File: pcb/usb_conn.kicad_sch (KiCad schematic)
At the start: 5 parts

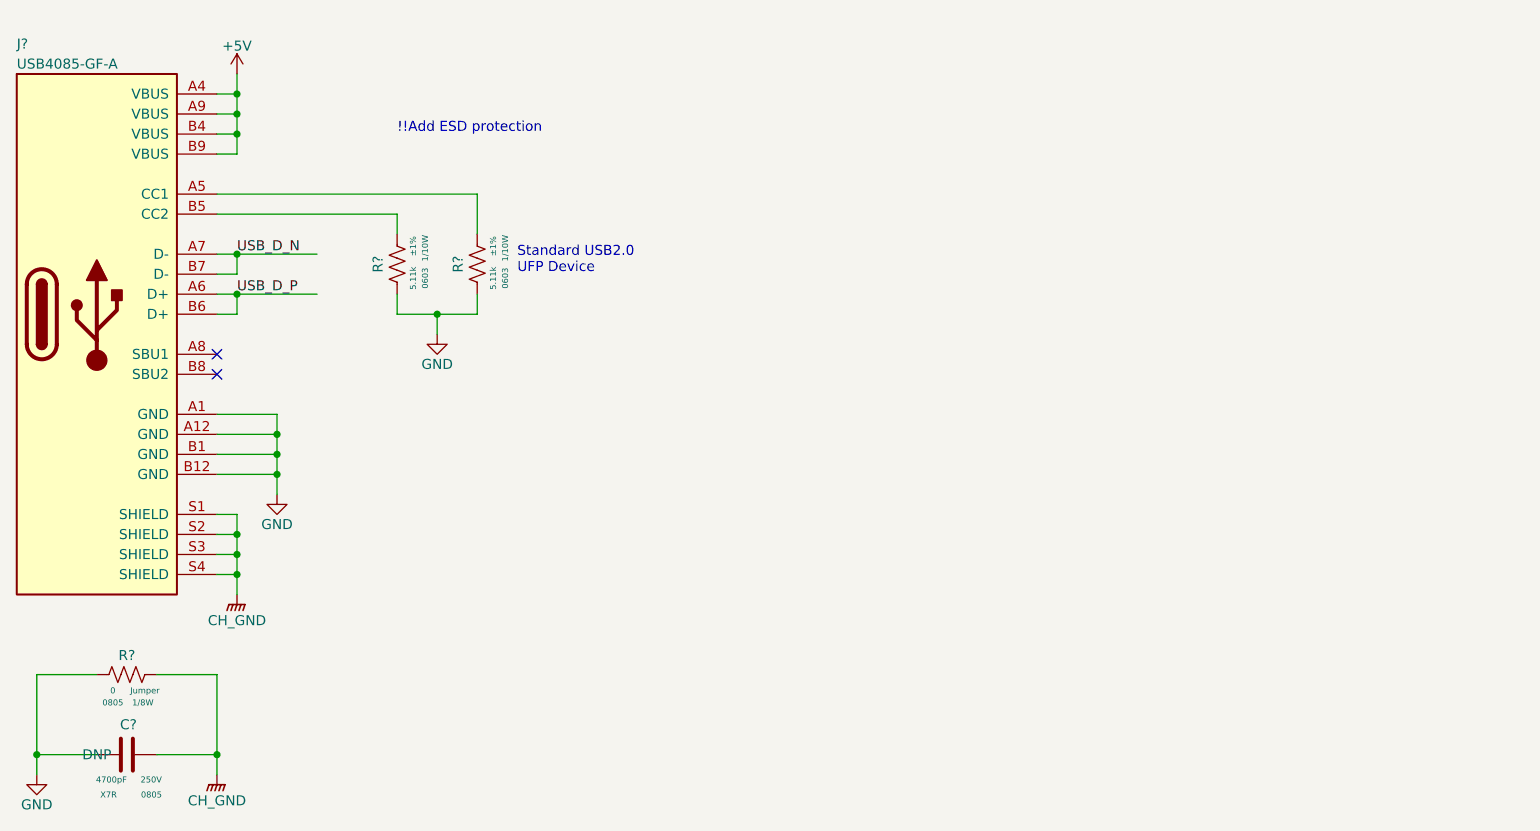
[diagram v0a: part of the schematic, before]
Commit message: Added IN-3 dots, picked FTDI chip and 3.3V LDO
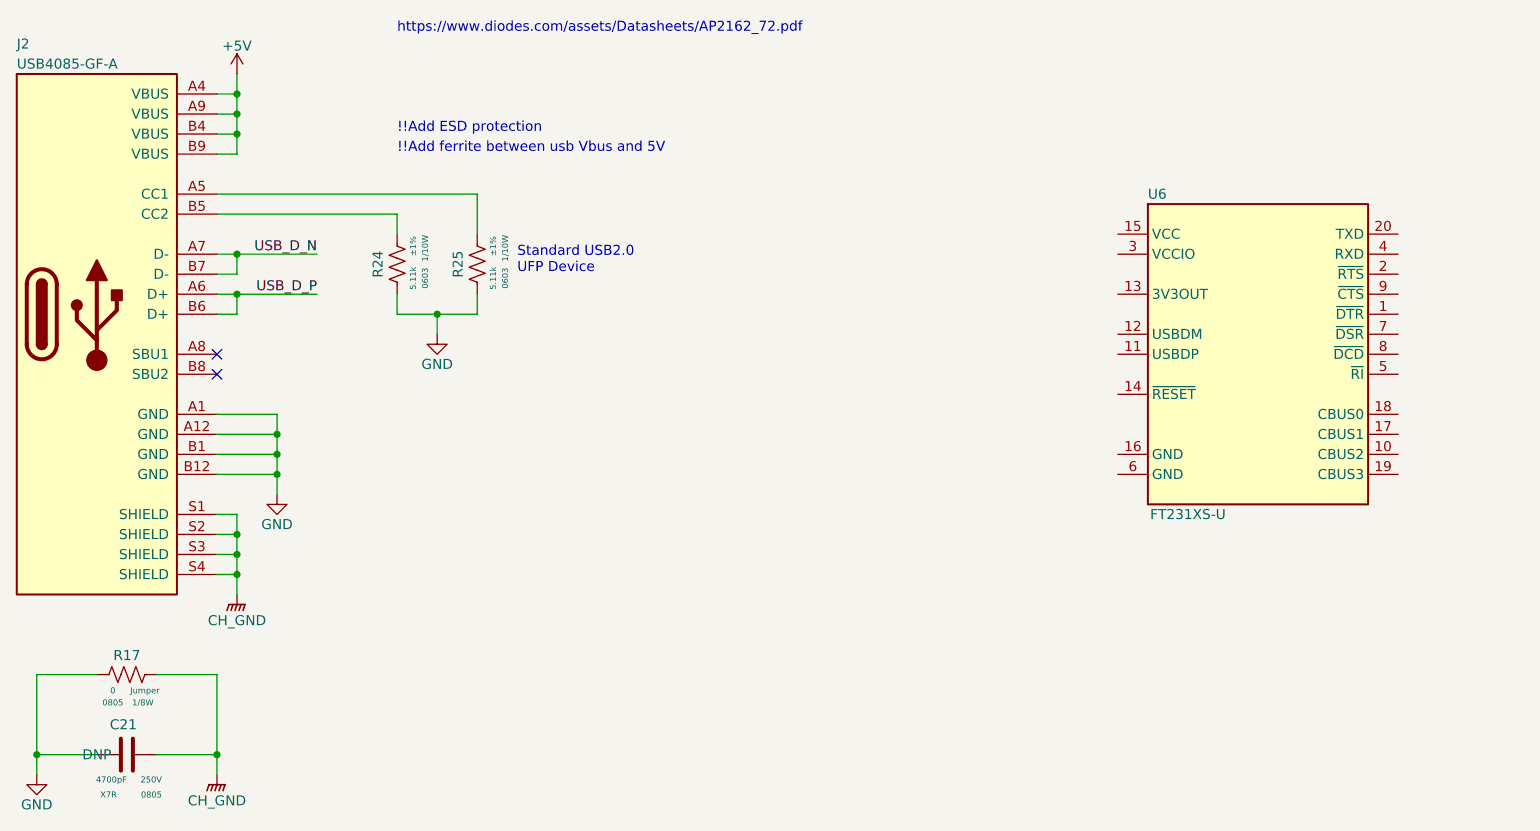
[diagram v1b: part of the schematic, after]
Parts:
- added U6: IC_FTDI_FT231XS, Package_SO:SSOP-20_3.9x8.7mm_P0.635mm, symbol arjun_symbols:IC_FTDI_FT231XS
- gave numbers to parts that had none: 5
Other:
- note added: "!!Add ferrite between usb Vbus and 5V"
- note added: "https://www.diodes.com/assets/Datasheets/AP2162_72.pdf"
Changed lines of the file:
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@@
+    (effects (font (size 1.27 1.27)) (justify left bottom))
+  )
+  (text "!!Add ferrite between usb Vbus and 5V" (at 78.74 71.12 0)
+    (effects (font (size 1.27 1.27)) (justify left bottom))
+  )
+  (text "https://www.diodes.com/assets/Datasheets/AP2162_72.pdf"
+    (at 78.74 55.88 0)
     (effects (font (size 1.27 1.27)) (justify left bottom))
   )
@@
     (effects (font (size 1.27 1.27)) (justify left bottom))
   )
-  (label "USB_D_P" (at 58.42 88.9 0)
-    (effects (font (size 1.27 1.27)) (justify left bottom))
-  )
-  (label "USB_D_N" (at 58.42 83.82 0)
-    (effects (font (size 1.27 1.27)) (justify left bottom))
+  (label "USB_D_P" (at 68.58 88.9 180)
+    (effects (font (size 1.27 1.27)) (justify right bottom))
+  )
+  (label "USB_D_N" (at 68.58 83.82 180)
+    (effects (font (size 1.27 1.27)) (justify right bottom))
   )
   (hierarchical_label "UART_BL_TX" (shape input) (at 251.46 93.98 0)
@@
   (symbol (lib_id "arjun_symbols:CH_GND") (at 58.42 127 0) (unit 1)
     (in_bom yes) (on_board yes)
-    (property "Reference" "#PWR?" (id 0) (at 58.42 132.08 0)
+    (property "Reference" "#PWR046" (id 0) (at 58.42 132.08 0)
       (effects (font (size 1.27 1.27)) hide)
     )
@@
   (symbol (lib_id "arjun_symbols:RES_5K11_1P_1{slash}10W_0603") (at 88.9 81.28 0) (unit 1)
     (in_bom yes) (on_board yes)
-    (property "Reference" "R?" (id 0) (at 85.725 85.09 90)
+    (property "Reference" "R25" (id 0) (at 85.725 85.09 90)
       (effects (font (size 1.27 1.27)) (justify top))
     )
@@
   (symbol (lib_id "power:+5V") (at 58.42 60.96 0) (unit 1)
     (in_bom yes) (on_board yes)
-    (property "Reference" "#PWR?" (id 0) (at 58.42 64.77 0)
+    (property "Reference" "#PWR045" (id 0) (at 58.42 64.77 0)
       (effects (font (size 1.27 1.27)) hide)
     )
@@
   (symbol (lib_id "arjun_symbols:RES_0R_1{slash}8W_0805") (at 48.26 137.16 270) (unit 1)
     (in_bom yes) (on_board yes)
-    (property "Reference" "R?" (id 0) (at 44.45 133.985 90)
+    (property "Reference" "R17" (id 0) (at 44.45 133.985 90)
       (effects (font (size 1.27 1.27)) (justify top))
     )
@@
   (symbol (lib_id "power:GND") (at 83.82 93.98 0) (unit 1)
     (in_bom yes) (on_board yes)
-    (property "Reference" "#PWR?" (id 0) (at 83.82 100.33 0)
+    (property "Reference" "#PWR055" (id 0) (at 83.82 100.33 0)
       (effects (font (size 1.27 1.27)) hide)
     )
@@
   (symbol (lib_id "arjun_symbols:CAP_CER_4700p_250V_X7R_0805") (at 40.64 147.32 90) (unit 1)
     (in_bom no) (on_board yes)
-    (property "Reference" "C?" (id 0) (at 45.72 143.51 90)
+    (property "Reference" "C21" (id 0) (at 45.72 143.51 90)
       (effects (font (size 1.27 1.27)) (justify left))
     )
@@
   (symbol (lib_id "arjun_symbols:CONN_USBC_RCPT_USB2.0_USB4085-GF-A") (at 55.88 63.5 0) (unit 1)
     (in_bom yes) (on_board yes)
-    (property "Reference" "J?" (id 0) (at 30.48 57.15 0)
+    (property "Reference" "J2" (id 0) (at 30.48 57.15 0)
       (effects (font (size 1.27 1.27)) (justify left))
     )
@@
   (symbol (lib_id "power:GND") (at 33.02 149.86 0) (unit 1)
     (in_bom yes) (on_board yes)
-    (property "Reference" "#PWR?" (id 0) (at 33.02 156.21 0)
+    (property "Reference" "#PWR043" (id 0) (at 33.02 156.21 0)
       (effects (font (size 1.27 1.27)) hide)
     )
@@
   (symbol (lib_id "arjun_symbols:RES_5K11_1P_1{slash}10W_0603") (at 78.74 81.28 0) (unit 1)
     (in_bom yes) (on_board yes)
-    (property "Reference" "R?" (id 0) (at 75.565 85.09 90)
+    (property "Reference" "R24" (id 0) (at 75.565 85.09 90)
       (effects (font (size 1.27 1.27)) (justify top))
     )
@@
   (symbol (lib_id "power:GND") (at 63.5 114.3 0) (unit 1)
     (in_bom yes) (on_board yes)
-    (property "Reference" "#PWR?" (id 0) (at 63.5 120.65 0)
+    (property "Reference" "#PWR047" (id 0) (at 63.5 120.65 0)
       (effects (font (size 1.27 1.27)) hide)
     )
@@
     (pin "1")
   )
+  (symbol (lib_id "arjun_symbols:IC_FTDI_FT231XS") (at 170.18 81.28 0) (unit 1)
+    (in_bom yes) (on_board yes)
+    (property "Reference" "U6" (id 0) (at 173.99 76.2 0)
+      (effects (font (size 1.27 1.27)) (justify left))
+    )
+    (property "Value" "IC_FTDI_FT231XS" (id 1) (at 231.14 63.5 0)
+      (effects (font (size 1.27 1.27)) (justify left) hide)
+    )
+    (property "Footprint" "Package_SO:SSOP-20_3.9x8.7mm_P0.635mm" (id 2) (at 254 66.04 0)
+      (effects (font (size 1.27 1.27)) hide)
+    )
+    (property "Datasheet" "https://www.ftdichip.com/Support/Documents/DataSheets/ICs/DS_FT231X.pdf" (id 3) (at 232.41 76.2 0)
+      (effects (font (size 1.27 1.27)) (justify left) hide)
+    )
+    (property "Manufacturer" "FTDI" (id 4) (at 232.41 78.74 0)
+      (effects (font (size 1.27 1.27)) (justify left) hide)
+    )
+    (property "ManufacturerPN" "FT231XS-U" (id 5) (at 179.07 116.84 0))
+    (property "Vendor" "Digi-Key" (id 6) (at 232.41 71.12 0)
+      (effects (font (size 1.27 1.27)) (justify left) hide)
+    )
+    (property "VendorPN" "768-1156-5-ND" (id 7) (at 232.41 73.66 0)
+      (effects (font (size 1.27 1.27)) (justify left) hide)
+    )
+    (pin "1")
+    (pin "10")
+    (pin "11")
+    (pin "12")
+    (pin "13")
+    (pin "14")
+    (pin "15")
+    (pin "16")
+    (pin "17")
+    (pin "18")
+    (pin "19")
+    (pin "2")
+    (pin "20")
+    (pin "3")
+    (pin "4")
+    (pin "5")
+    (pin "6")
+    (pin "7")
+    (pin "8")
+    (pin "9")
+  )
   (symbol (lib_id "arjun_symbols:CH_GND") (at 55.88 149.86 0) (unit 1)
     (in_bom yes) (on_board yes)
-    (property "Reference" "#PWR?" (id 0) (at 55.88 154.94 0)
-      (effects (font (size 1.27 1.27)) hide)
-    )
+    (property "Reference" "#PWR044" (id 0) (at 55.88 154.94 0)
+      (effects (font (size 1.27 1.27)) hide)
+    )

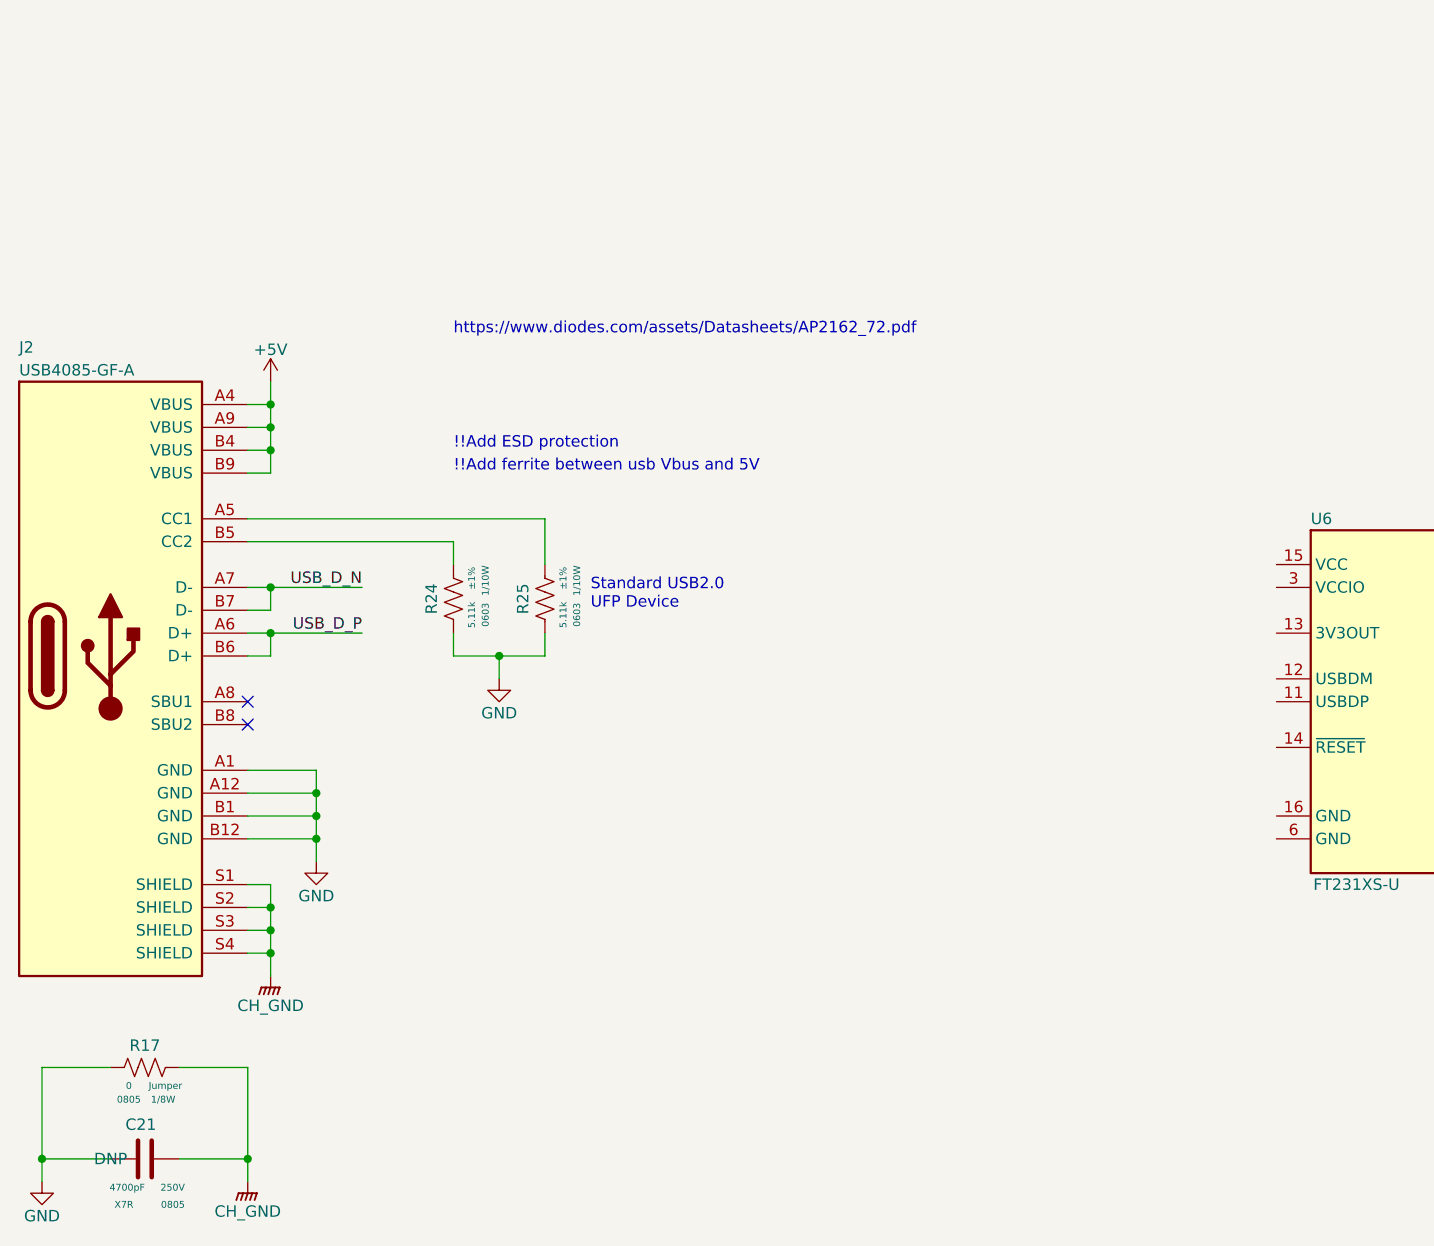
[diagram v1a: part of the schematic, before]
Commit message: Finished 12V boost circuit and updated sim to match
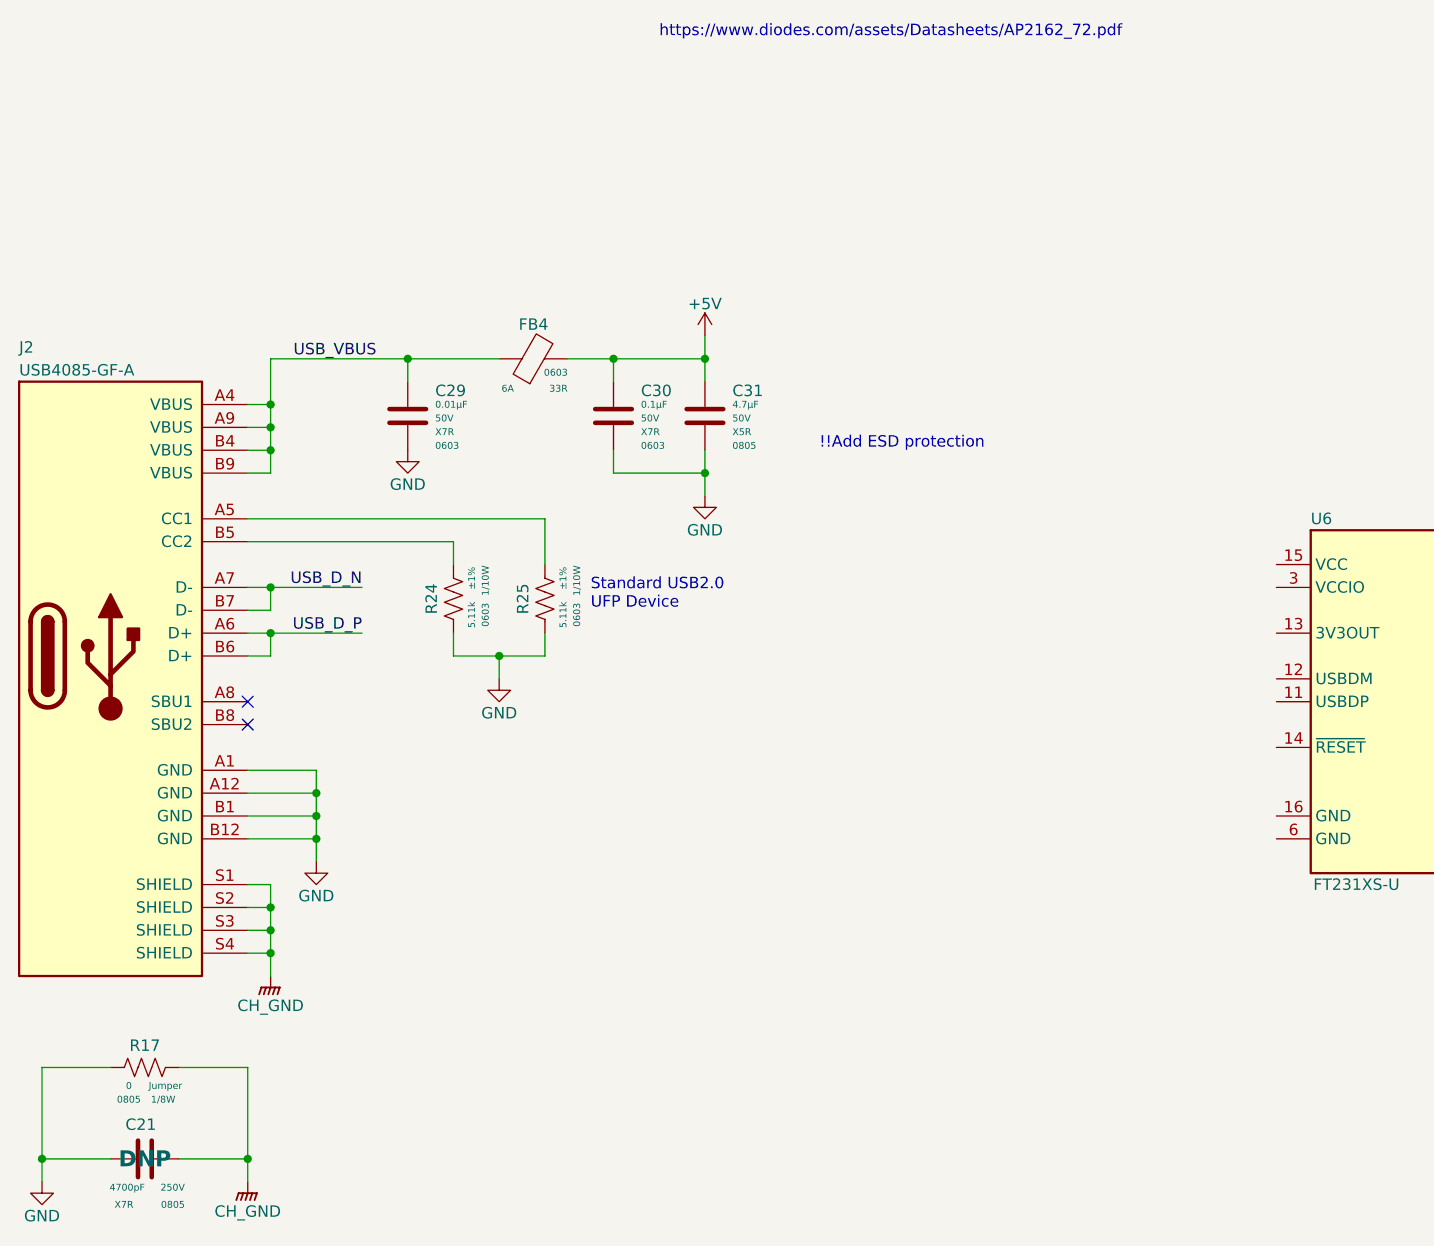
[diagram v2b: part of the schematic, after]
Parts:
- added C29: CAP_CER_0u01_50V_X7R_0603, Capacitor_SMD:C_0603_1608Metric, symbol .arjun:CAP_CER_0u01_50V_X7R_0603
- added C30: CAP_CER_0u1_50V_X7R_0603, Capacitor_SMD:C_0603_1608Metric, symbol .arjun:CAP_CER_0u1_50V_X7R_0603
- added C31: CAP_CER_4u7_50V_X5R_0805, Capacitor_SMD:C_0805_2012Metric, symbol .arjun:CAP_CER_4u7_50V_X5R_0805
- added FB4: FER_33R_6A_0603, Inductor_SMD:L_0603_1608Metric, symbol .arjun:FER_33R_6A_0603
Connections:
- net +5V: now also C30.1, C31.1, FB4.2; no longer J2.A4 (VBUS), J2.A9 (VBUS), J2.B4 (VBUS), J2.B9 (VBUS)
- net GND: now also C29.2, C30.2, C31.2
- new net USB_VBUS: C29.1, FB4.1, J2.A4 (VBUS), J2.A9 (VBUS), J2.B4 (VBUS), J2.B9 (VBUS)
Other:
- note removed: "!!Add ferrite between usb Vbus and 5V"
